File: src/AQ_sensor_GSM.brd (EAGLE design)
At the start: 110 x 64 mm, 75 parts, among them IC1 MIC29302WU, IC2 MCP73831/OT, J1 F-1X03-SIP-100-32, J2 SIM8060-6-1-14-00-A, Q1 MMBT2222, SW1 PCM12SMTR, SW2 PCM12SMTR, U2 TEXAS_INSTRUMENTS_SN74HC125TE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, U3 TEXAS_INSTRUMENTS_LM1117IMP-3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, U4 EC200UCNAB-N05-SNNSA, X1 53048-08, X4 50 Ohms

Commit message: Added GNSS Antenna, reconfigured the PCB Layout
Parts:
- removed S1: KMR621NGLFS, AQ_sensor_GSM:SW_KMR621NGLFS
- removed SW1, SW2: PCM12SMTR, AQ_sensor_GSM:SW_PCM12SMTR
- removed U1: (no value), AQ_sensor_GSM:SIM800L
- removed X4: 50 Ohms, AQ_sensor_GSM:SMA_EDGELAUNCH_UFL
- added ESP_RESET, GSM_RST: KMR621NGLFS, AQ_sensor_GSM:SW_KMR621NGLFS
- added GPS, GSM: 50 Ohms, AQ_sensor_GSM:SMA_EDGELAUNCH_UFL
- added POWER_SW: PCM12SMTR, AQ_sensor_GSM:SW_PCM12SMTR
- added Q2, Q3: MMBT2222, MMBT2222_:SOT23-BEC
- added R15, R21: 4.7K, rcl:R0603
- added R18, R22: 47K, rcl:R0603
- moved C13 263.8 mm to (101.6, 55.7), flipped to the bottom, turned to 270 degrees
- moved C14 262.4 mm to (97.9, 53.5), turned to 90 degrees
- moved 51K 259.5 mm to (37.0, 46.9)
- moved C12 253.9 mm to (97.1, 55.2), flipped to the bottom, turned to 90 degrees
- moved J2 247.0 mm to (25.9, 56.1), turned to 270 degrees
- moved D5 243.1 mm to (90.3, 51.5), flipped to the bottom, turned to 90 degrees
- moved C7 238.9 mm to (86.8, 51.4), flipped to the bottom, turned to 270 degrees
- moved R12 235.9 mm to (82.2, 56.2), flipped to the bottom, turned to 90 degrees
- moved R13 231.2 mm to (82.4, 51.2), flipped to the bottom, turned to 270 degrees
- moved C18 228.1 mm to (16.1, 47.0), turned to 90 degrees
- moved C17 226.4 mm to (12.0, 51.9)
- moved C16 226.1 mm to (12.0, 56.4)
- moved C15 217.7 mm to (6.80, 54.6), turned to 180 degrees
- moved 10K 212.0 mm to (11.9, 47.5)
- moved C6 211.3 mm to (68.8, 54.5), turned to 270 degrees
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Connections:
- net N$29 renamed BT_ANT
- removed net N$26: U4.20
- removed net N$28: U4.47
- removed net N$30: U4.49
- removed net VBUS: U1.7
- new net GNSS_ANT: GPS.P, U4.47
- new net N$1: Q2.B, R15.2, R18.2
- new net N$18: SV2.8
- new net N$19: SV2.9
- new net N$2: Q3.B, R21.2, R22.2
- new net N$20: SV2.10
- new net N$21: SV2.11
- new net N$22: SV2.12
- new net PWRKEY_0: R21.1, SV1.15
- net +3V3: now also SV1.10
- net +5V: now also POWER_SW.1; no longer SW1.1
- net 1.8V: no longer U1.16
- net 2.8V: no longer U1.18
- net ESP_RST: now also ESP_RESET.2_1, ESP_RESET.2_2; no longer SW2.2
- net GND: now also ESP_RESET.1_1, ESP_RESET.1_2, GPS.GND@1, GPS.GND@2, GPS.GND@3, GPS.GND@4, GSM.GND@1, GSM.GND@2, GSM.GND@3, GSM.GND@4, GSM_RST.1_1, GSM_RST.1_2, POWER_SW.S1, POWER_SW.S2, POWER_SW.S3, POWER_SW.S4, Q2.E, Q3.E, R18.1, R22.1, SV1.9; no longer S1.1_1, S1.1_2, SW1.S1, SW1.S2, SW1.S3, SW1.S4, SW2.1, SW2.S1, SW2.S2, SW2.S3, SW2.S4, U1.2, U1.35, U1.37, U1.38, U1.39, U1.41, U1.43, U1.44, U1.45, U1.58, U1.6, U1.67, U1.71, U1.72, U1.73, U1.76, U1.77, U1.78, U1.79, U1.8, U1.80, U1.81, U1.82, U1.83, U1.84, U1.85, U1.86, U1.87, U1.88, X4.GND@1, X4.GND@2, X4.GND@3, X4.GND@4
- net GSM_ANT: now also GSM.P, U4.49; no longer U1.40, X4.P
- net GSM_RST: now also Q2.C, U4.20; no longer U1.49
- net GSM_RST_O: now also R15.1
- net GSM_RX: no longer U1.31
- net GSM_TX: no longer U1.32
- net NETSTAT: no longer U1.64
- net PWRKEY: now also GSM_RST.2_1, GSM_RST.2_2, Q3.C; no longer S1.2_1, S1.2_2, U1.48
- net PWRSTAT: no longer U1.4
- net RI: no longer U1.68
- net SIMCLK: no longer U1.55
- net SIMDATA: no longer U1.14
- net SIMRST: no longer U1.15
- net VBAT_EN: now also SV2.7
- net VIN: now also POWER_SW.2; no longer SW1.2
- net VRTC: no longer U1.56
- net V_LIPO: no longer U1.1, U1.42
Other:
- board text removed: "POWER"
- board text removed: "RESET"
- board text removed: "SWITCH"

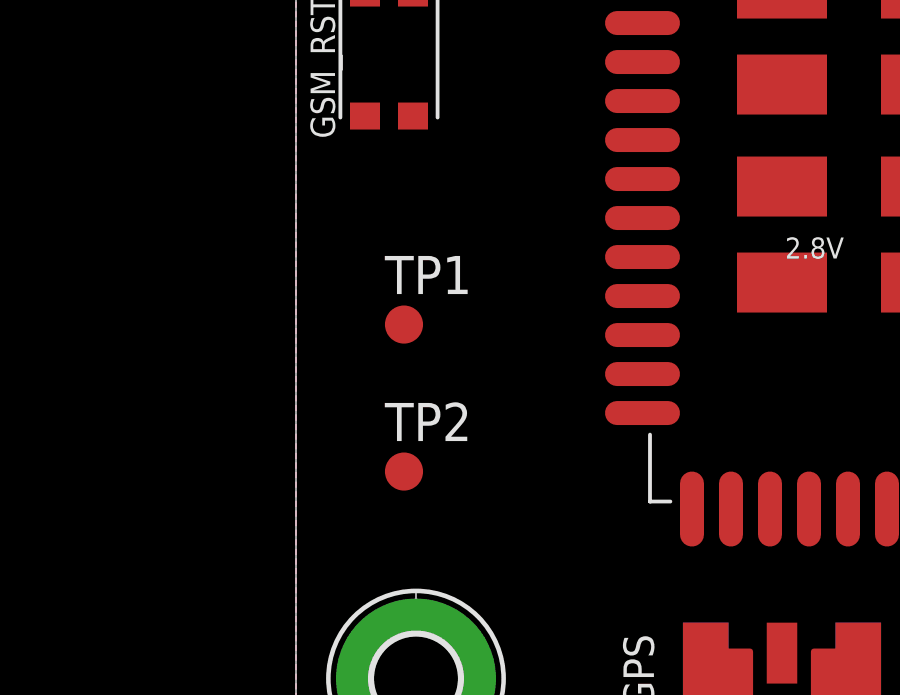
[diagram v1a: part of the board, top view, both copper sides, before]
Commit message: Added Bluetooth and Wifi Antenna
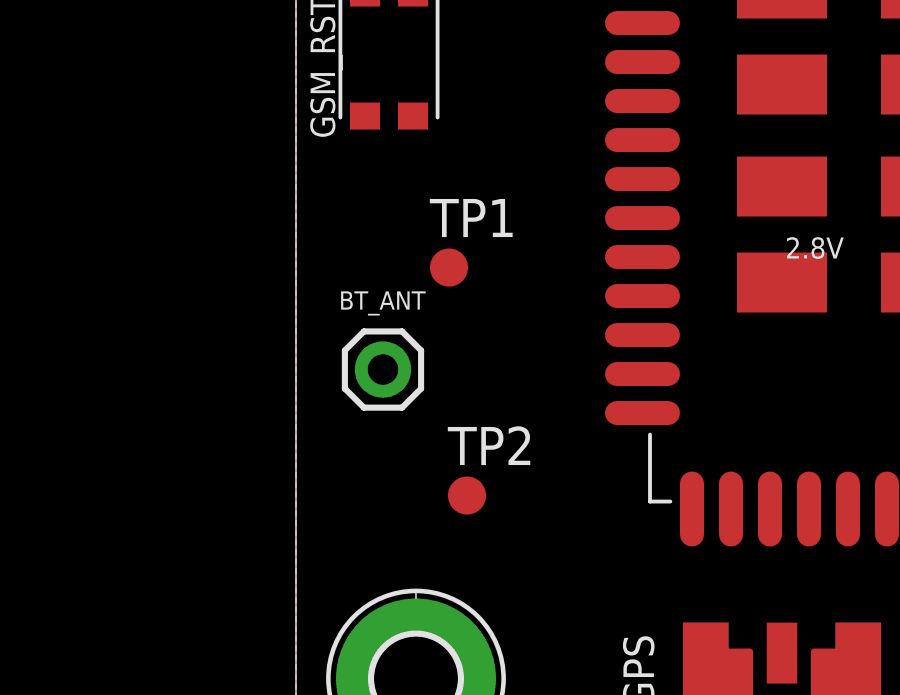
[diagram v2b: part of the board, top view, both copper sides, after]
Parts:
- added BT_ANT: (no value), SparkFun-Connectors:1X01
- moved TP1 2.42 mm to (5.10, 17.7)
- moved TP2 2.25 mm to (5.70, 10.1)
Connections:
- net BT_ANT: now also BT_ANT.1

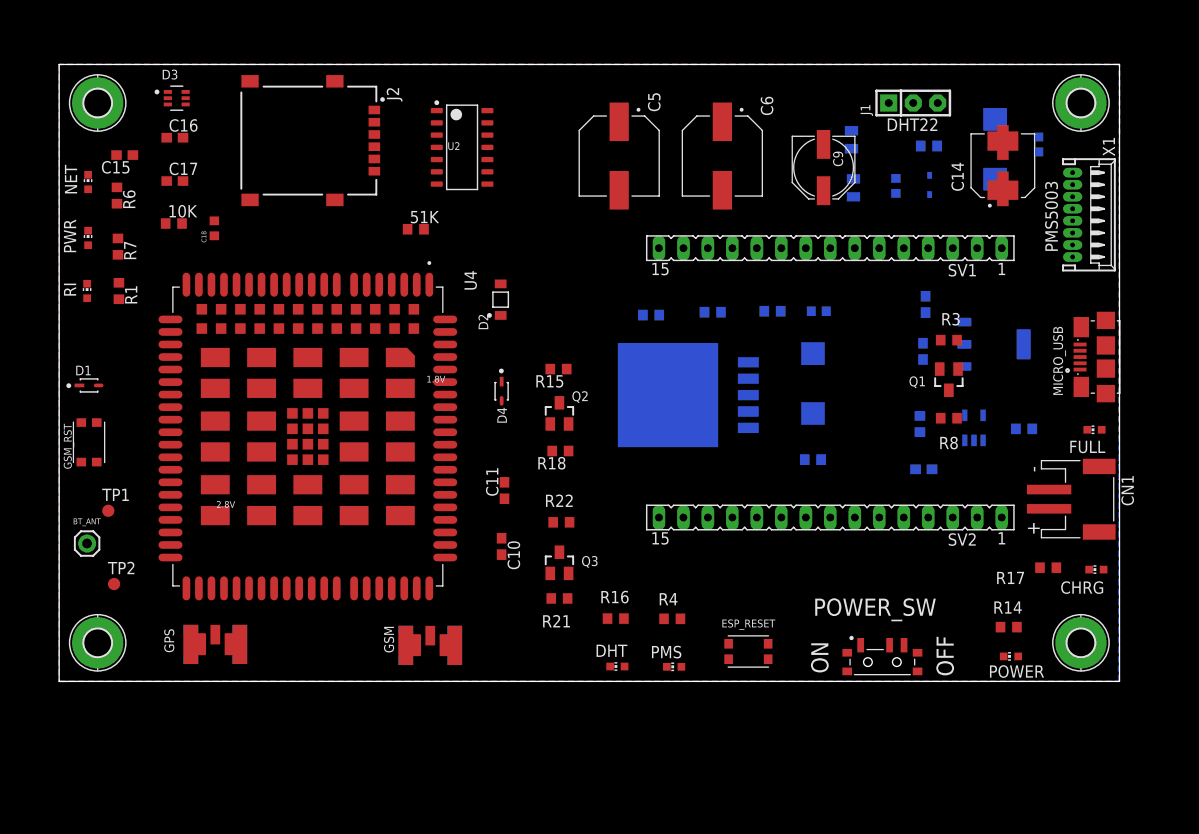
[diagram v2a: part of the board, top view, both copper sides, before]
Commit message: Updated GSM antenna positions, pms connector, USB, and battery connector positions
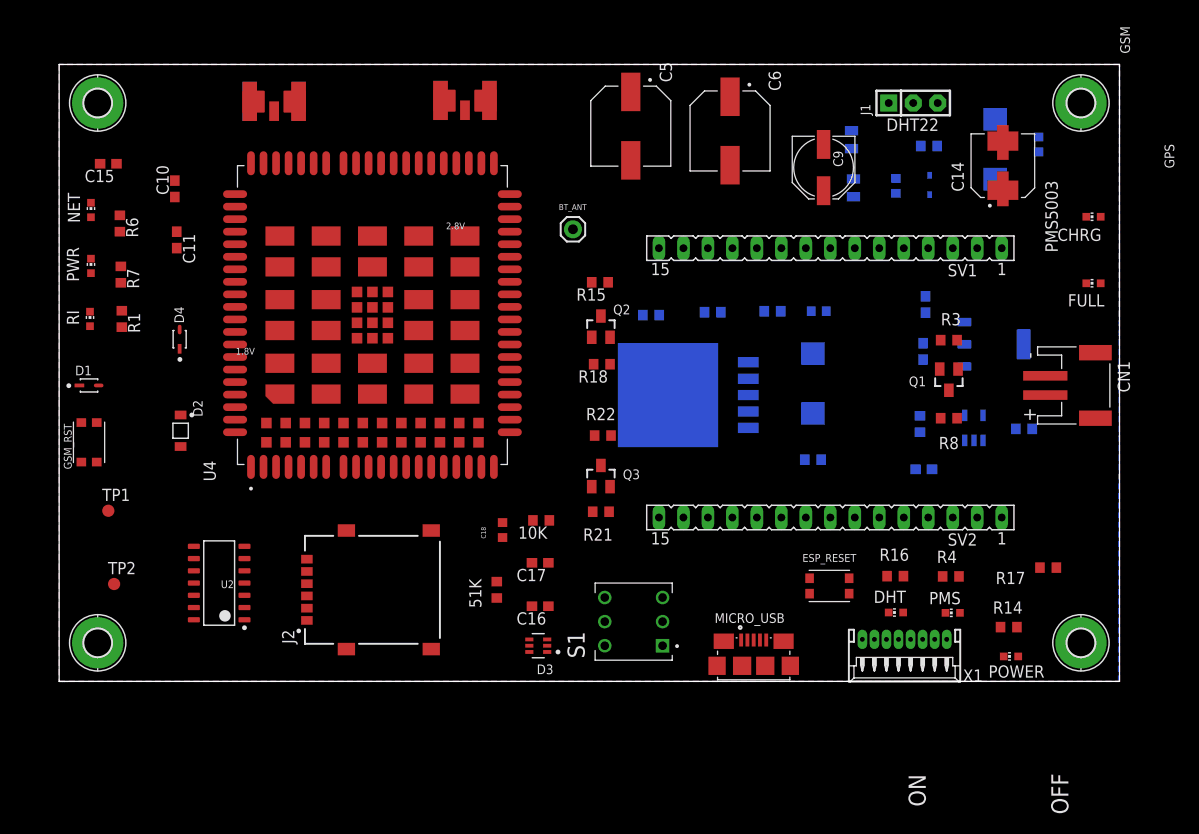
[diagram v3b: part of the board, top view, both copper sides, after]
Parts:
- removed POWER_SW: PCM12SMTR, AQ_sensor_GSM:SW_PCM12SMTR
- added S1: TL2285EE, TL2285EE:SW_TL2285EE
- moved D3 68.1 mm to (49.7, 3.70), turned to 180 degrees
- moved GPS 65.8 mm to (42.1, 62.3), turned to 270 degrees
- moved GSM 62.6 mm to (22.3, 62.2), turned to 270 degrees
- moved C16 61.6 mm to (49.9, 7.80), turned to 180 degrees
- moved BT_ANT 60.0 mm to (53.3, 46.9)
- moved C17 54.8 mm to (49.9, 12.3), turned to 180 degrees
- moved U2 51.8 mm to (16.6, 10.2), turned to 180 degrees
- moved C10 50.3 mm to (12.0, 51.1), turned to 90 degrees
- moved X1 49.0 mm to (87.7, 3.11), turned to 180 degrees
- moved 10K 49.0 mm to (50.0, 16.7), turned to 180 degrees
- moved J2 47.1 mm to (32.5, 9.50), turned to 90 degrees
- moved MICRO_USB 44.8 mm to (72.0, 4.29), turned to 0 degrees
- moved C18 43.3 mm to (46.0, 15.7)
- moved C11 42.8 mm to (12.2, 45.8), turned to 270 degrees
- moved 51K 38.3 mm to (45.4, 9.50), turned to 270 degrees
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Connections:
- removed net VIN: MICRO_USB.1, POWER_SW.2
- new net N$17: MICRO_USB.1, S1.3, S1.4
- net +5V: now also S1.2, S1.5; no longer POWER_SW.1
- net GND: no longer POWER_SW.S1, POWER_SW.S2, POWER_SW.S3, POWER_SW.S4

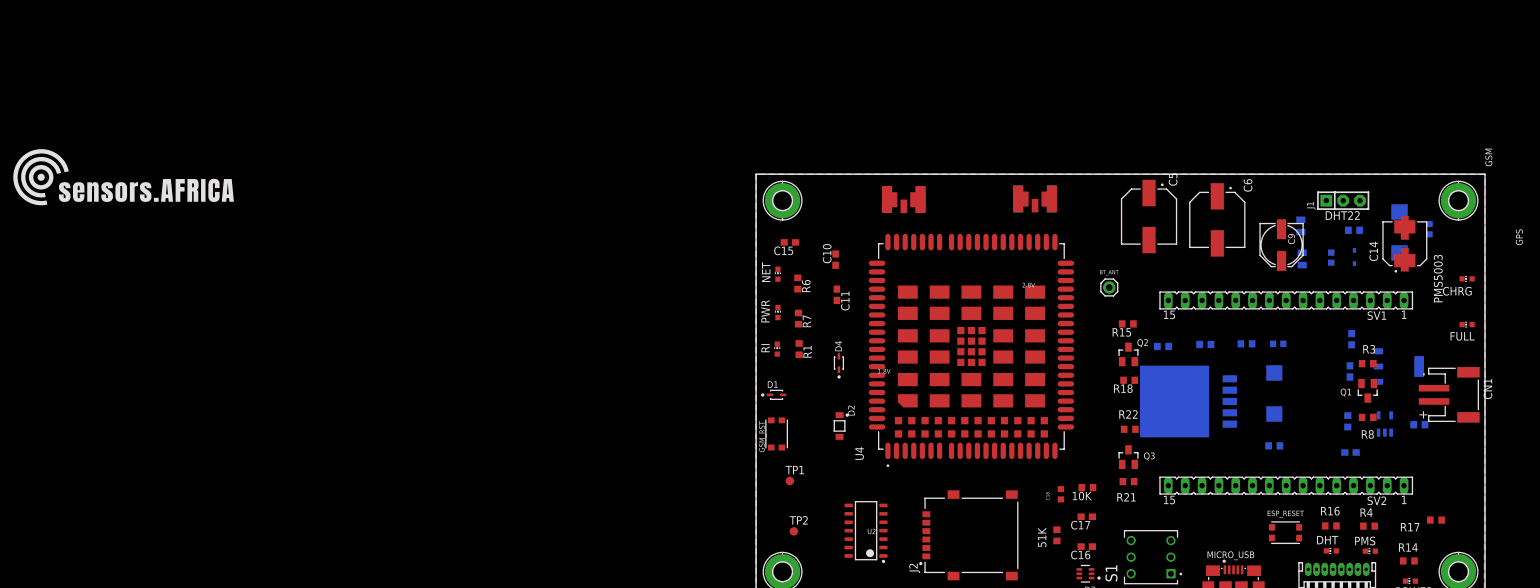
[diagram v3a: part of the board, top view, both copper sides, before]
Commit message: Added dC jack
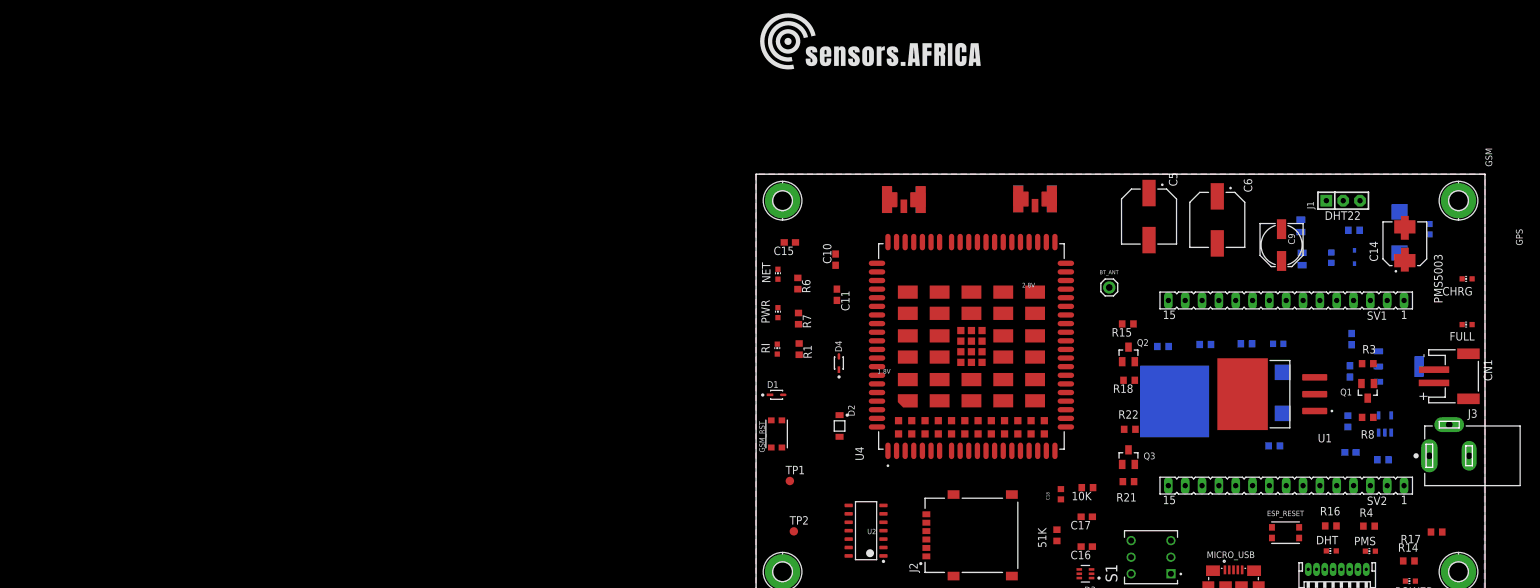
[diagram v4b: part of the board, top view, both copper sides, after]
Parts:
- added J3: PJ-002BH, PJ-002BH:CUI_PJ-002BH
- added U1: LM7805S/NOPB, LM7805S_NOPB:TO254P1524X483-4N
- moved R19 7.64 mm to (94.6, 20.9)
- moved CN1 2.80 mm to (106.0, 33.5)
- moved R17 1.80 mm to (102.7, 10.0)
- moved C2 1.30 mm to (79.5, 31.0)
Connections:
- new net N$24: J3.1, U1.1
- net +5V: now also U1.3
- net GND: now also J3.2, J3.3, U1.2, U1.4

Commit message: PCB Routed
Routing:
- net +5V: track 0.00 -> 286.1 mm, vias 0 -> 5
- net V_LIPO: track 0.00 -> 146.3 mm, vias 0 -> 5
- net SIMDATA: track 0.00 -> 103.5 mm, vias 0 -> 3
- net GSM_RX_O: track 0.00 -> 95.6 mm, vias 0 -> 1
- net PMS_RX: track 0.00 -> 81.2 mm, vias 0 -> 2
- net GSM_TX_5V: track 0.00 -> 77.1 mm, vias 0 -> 1
- net N$34: track 0.00 -> 69.9 mm, vias 0 -> 2
- net N$39: track 0.00 -> 67.9 mm, vias 0 -> 4
- net PWRKEY: track 0.00 -> 67.8 mm, vias 0 -> 4
- net +3V3: track 0.00 -> 63.1 mm
- net PMS_TX: track 0.00 -> 62.4 mm, vias 0 -> 2
- net PMS_LED: track 0.00 -> 61.6 mm, vias 0 -> 3
- net USIM_VDD: track 0.00 -> 56.7 mm
- net NETSTAT_5V: track 0.00 -> 53.3 mm, vias 0 -> 2
- net DHT_LED: track 0.00 -> 52.1 mm, vias 0 -> 2
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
